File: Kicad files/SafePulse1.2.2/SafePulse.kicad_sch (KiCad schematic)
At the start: 87 parts, among them J1 Conn_01x03_Male, Q1 FQT7N10L, Q2 BC846A, Q3 MMBT3906, Q4 MMBT3906, U1 TS4061AILT-1.25, U2 74HC14, U3 TLV27L1DBVT, U33 MAX9910EXK+T, U4 CD14538BM

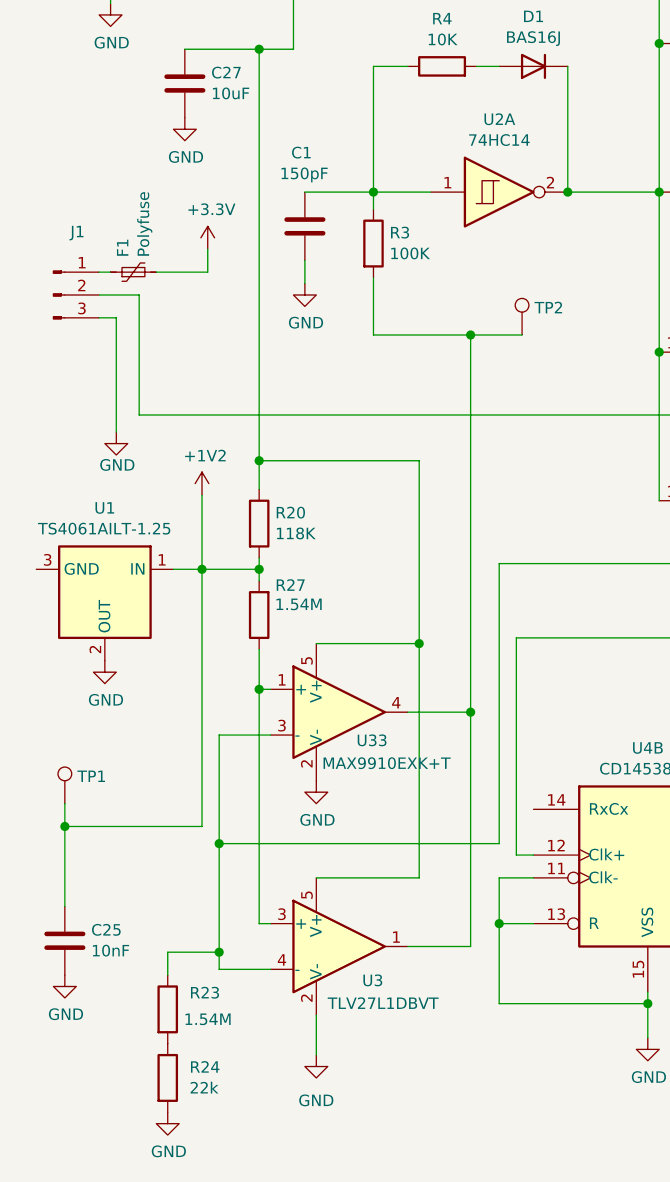
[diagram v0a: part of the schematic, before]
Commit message: Updated Schematic and Board with new C1 and new R24 values
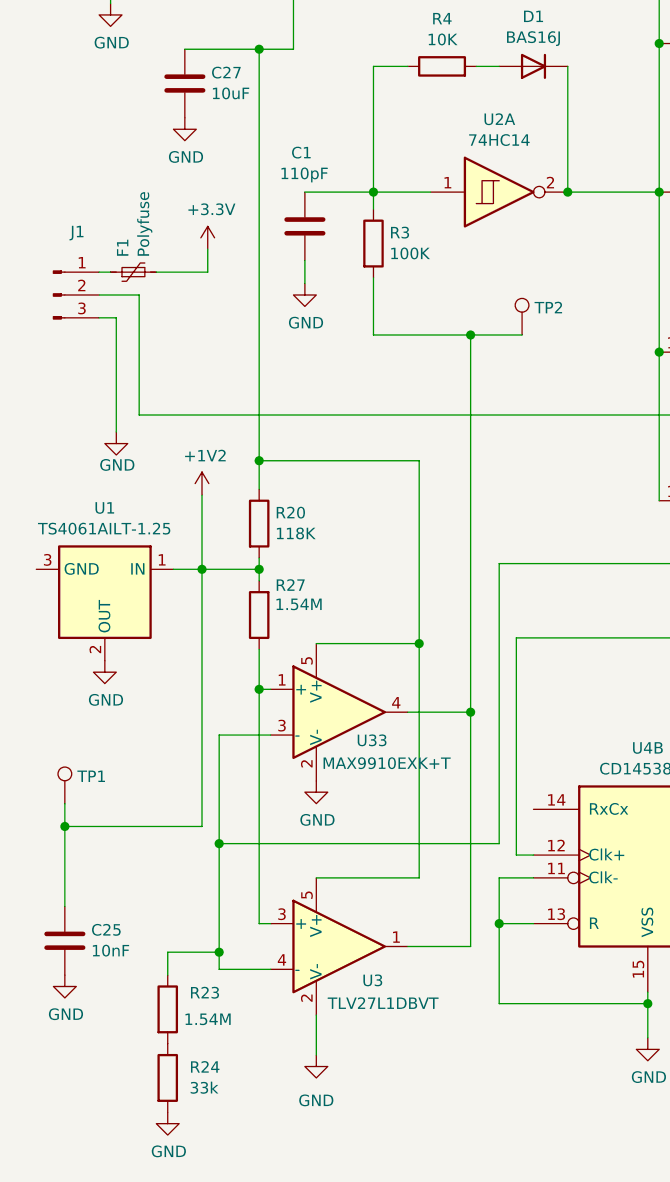
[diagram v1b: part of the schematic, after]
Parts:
- C1: value 150pF -> 110pF
- R24: value 22k -> 33k
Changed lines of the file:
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@@
-(kicad_sch (version 20210406) (generator eeschema)
+(kicad_sch (version 20210621) (generator eeschema)
   (paper "A4")
   (title_block
@@
       (effects (font (size 1.27 1.27)) (justify left))
     )
-    (property "Value" "22k" (id 1) (at 32.893 187.833 0)
+    (property "Value" "33k" (id 1) (at 32.893 187.833 0)
       (effects (font (size 1.27 1.27)) (justify left))
     )
@@
       (effects (font (size 1.27 1.27)) (justify left))
     )
-    (property "Value" "150pF" (id 1) (at 42.926 86.233 0)
+    (property "Value" "110pF" (id 1) (at 42.926 86.233 0)
       (effects (font (size 1.27 1.27)) (justify left))
     )
@@
     )
     (path "/00000000-0000-0000-0000-0000600fa622"
-      (reference "C1") (unit 1) (value "150pF") (footprint "Capacitor_SMD:C_0805_2012Metric")
+      (reference "C1") (unit 1) (value "110pF") (footprint "Capacitor_SMD:C_0805_2012Metric")
     )
     (path "/00000000-0000-0000-0000-0000600aa140"
@@
     )
     (path "/95ffa48f-5e4a-4d1a-b1a7-fe360b6ab119"
-      (reference "R24") (unit 1) (value "22k") (footprint "Resistor_SMD:R_0805_2012Metric")
+      (reference "R24") (unit 1) (value "33k") (footprint "Resistor_SMD:R_0805_2012Metric")
     )
     (path "/6262f35d-33c6-4702-969c-2648bf6ad569"
